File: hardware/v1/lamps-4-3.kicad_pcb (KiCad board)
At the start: 2 copper layers, 169.5 x 26 mm, 14 parts, among them P1 CONN_01X04, P2 CONN_01X04, P3 CONN_02X05

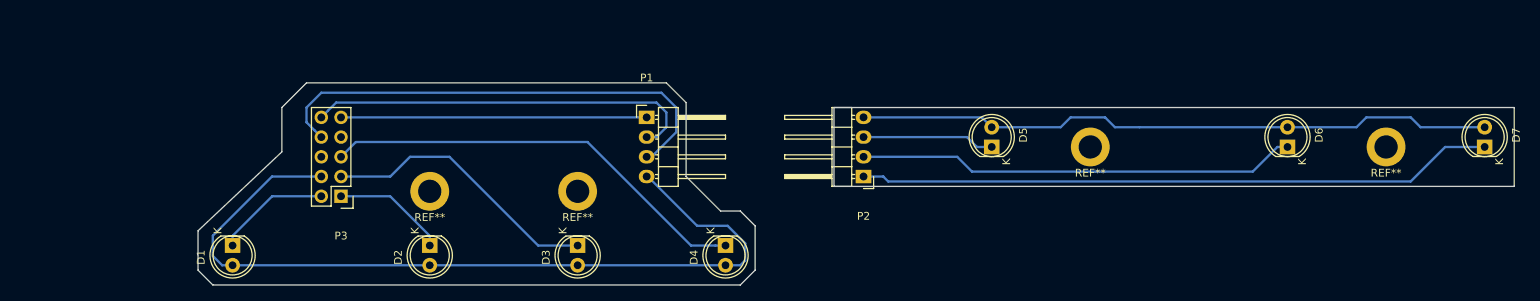
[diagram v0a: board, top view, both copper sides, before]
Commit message: Correct dial size (sources say 3 inch or 78mm - settled for 77 now), and reduce size of board for lights-4-3 (4 part).
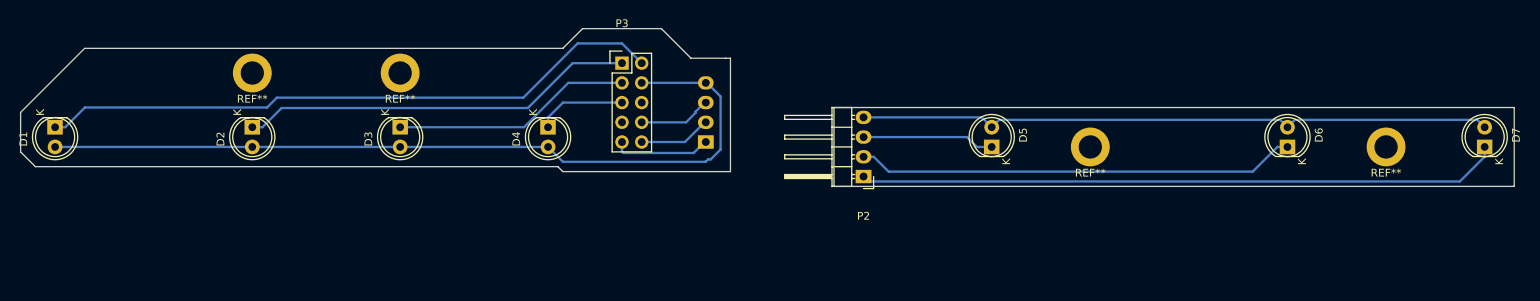
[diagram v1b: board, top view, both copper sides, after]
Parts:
- P1: moved to B.Cu
- moved P3 40.1 mm to (104.8, 65.4), turned to 0 degrees
- moved D2 27.5 mm to (57.1, 73.7)
- moved REF** 27.5 mm to (57.1, 66.7)
- moved D1 27.5 mm to (31.8, 73.7)
- moved D3 27.5 mm to (76.2, 73.7)
- moved D4 27.5 mm to (95.2, 73.7)
- moved REF** 27.5 mm to (76.2, 66.7)
- moved P1 8.25 mm to (115.6, 75.6)
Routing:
- net /SEG0: track 14.8 -> 81.1 mm
- net /SEG7: track 62.1 -> 9.40 mm
- net /SEG3: track 55.8 -> 11.6 mm
- net /SEG6: track 50.7 -> 9.31 mm
- net /SEG1: track 14.8 -> 51.0 mm
- net /SEG5: track 39.4 -> 12.7 mm
- net /SEG2: track 36.3 -> 30.9 mm
- net /DIGITA: track 107.5 -> 104.9 mm
- net Net-(D7-Pad1): track 82.1 -> 82.8 mm
- net Net-(D5-Pad2): track 82.8 -> 82.1 mm
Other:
- board size 169.5 x 26 mm -> 192.4 x 20.3 mm
